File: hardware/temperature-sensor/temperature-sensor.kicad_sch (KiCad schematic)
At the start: 0 parts

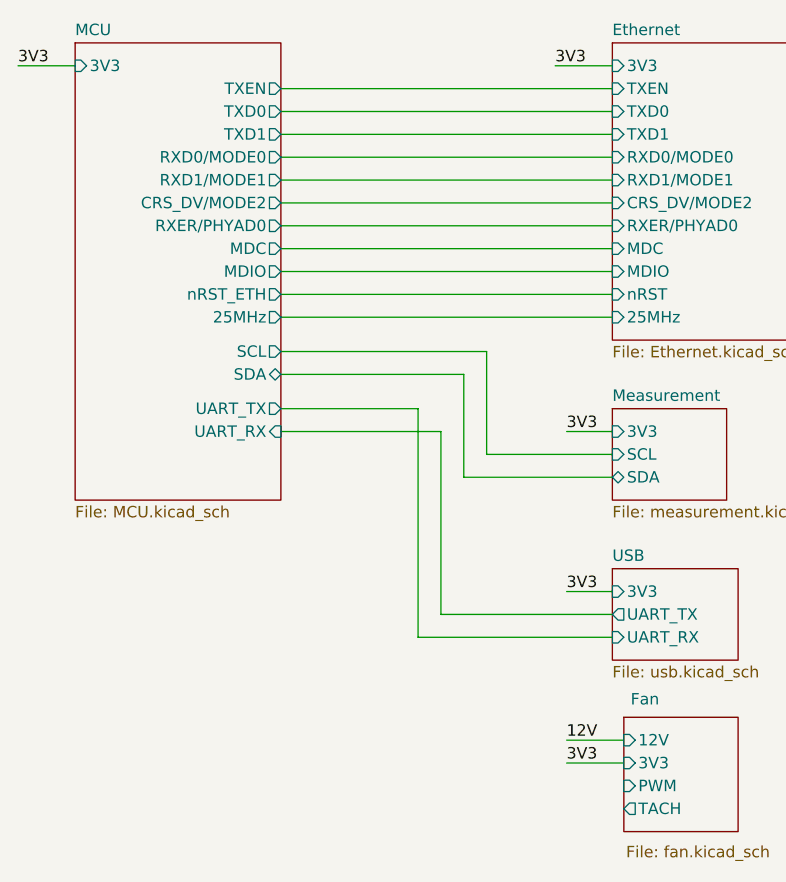
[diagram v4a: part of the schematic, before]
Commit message: add connection to FAN PWM and TACH
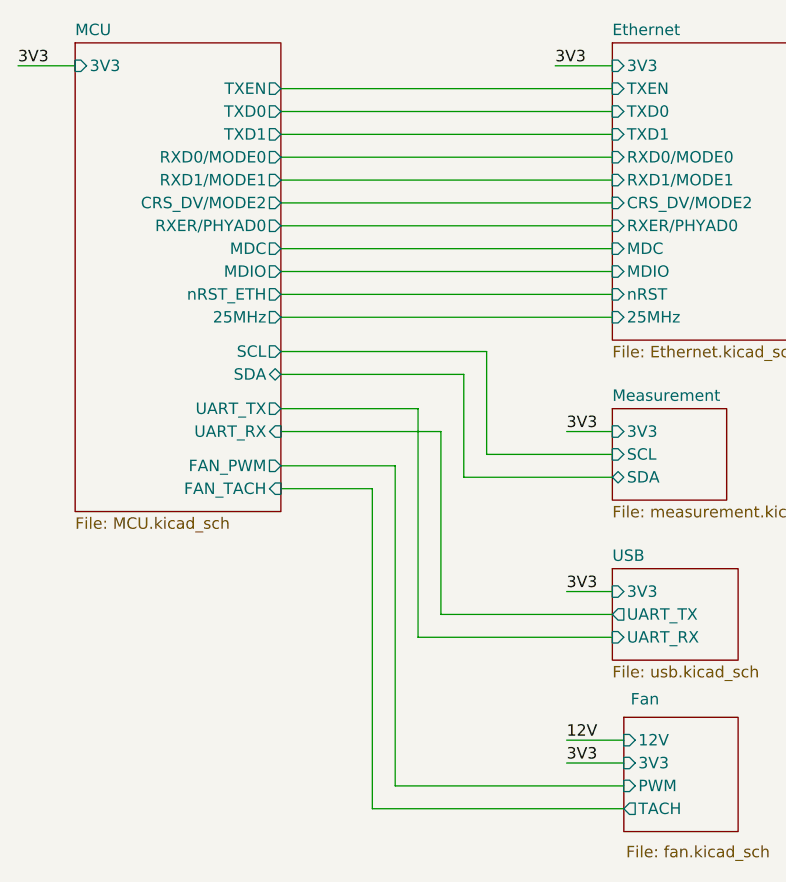
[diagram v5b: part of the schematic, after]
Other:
- sheet MCU ports: added FAN_PWM, FAN_TACH; removed none
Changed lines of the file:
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@@
+	(wire
+		(pts
+			(xy 115.57 77.47) (xy 105.41 77.47)
+		)
+		(stroke
+			(width 0)
+			(type default)
+		)
+	)
 	(wire
 		(pts
@@
 	(wire
 		(pts
+			(xy 143.51 110.49) (xy 118.11 110.49)
+		)
+		(stroke
+			(width 0)
+			(type default)
+		)
+	)
+	(wire
+		(pts
 			(xy 120.65 93.98) (xy 120.65 68.58)
 		)
@@
 	(wire
 		(pts
+			(xy 118.11 74.93) (xy 105.41 74.93)
+		)
+		(stroke
+			(width 0)
+			(type default)
+		)
+	)
+	(wire
+		(pts
 			(xy 168.91 30.48) (xy 177.8 30.48)
 		)
@@
 	(wire
 		(pts
+			(xy 143.51 113.03) (xy 115.57 113.03)
+		)
+		(stroke
+			(width 0)
+			(type default)
+		)
+	)
+	(wire
+		(pts
 			(xy 105.41 64.77) (xy 125.73 64.77)
 		)
@@
 	(wire
 		(pts
+			(xy 118.11 110.49) (xy 118.11 74.93)
+		)
+		(stroke
+			(width 0)
+			(type default)
+		)
+	)
+	(wire
+		(pts
 			(xy 137.16 107.95) (xy 143.51 107.95)
 		)
@@
 		(pts
 			(xy 105.41 33.02) (xy 142.24 33.02)
+		)
+		(stroke
+			(width 0)
+			(type default)
+		)
+	)
+	(wire
+		(pts
+			(xy 115.57 113.03) (xy 115.57 77.47)
 		)
 		(stroke
@@
 	(sheet
 		(at 82.55 27.94)
-		(size 22.86 50.8)
+		(size 22.86 52.07)
 		(fields_autoplaced yes)
 		(stroke
@@
 		)
 		(property "Sheetfile" "MCU.kicad_sch"
-			(at 82.55 79.3246 0)
+			(at 82.55 80.5946 0)
 			(effects
 				(font
@@
 			(effects
 				(font
+					(size 1.27 1.27)
+				)
+				(justify right)
+			)
+		)
+		(pin "FAN_PWM" output
+			(at 105.41 74.93 0)
+			(effects
+				(font
+					(size 1.27 1.27)
+				)
+				(justify right)
+			)
+		)
+		(pin "FAN_TACH" input
+			(at 105.41 77.47 0)
+			(effects
+				(font
